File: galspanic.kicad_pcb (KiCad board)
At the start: 2 copper layers, 86.5 x 150 mm, 28 parts, among them J1 x68000_expansion, U1 CY62167E, U10 SN74AHCT245, U11 SN74AHCT245, U2 CY62167E, U3 CY62167E, U4 CY62167E, U5 ATF22V10C-10PU, U6 SN74AHCT245, U7 SN74AHCT245, U8 SN74AHCT245, U9 SN74AHCT245

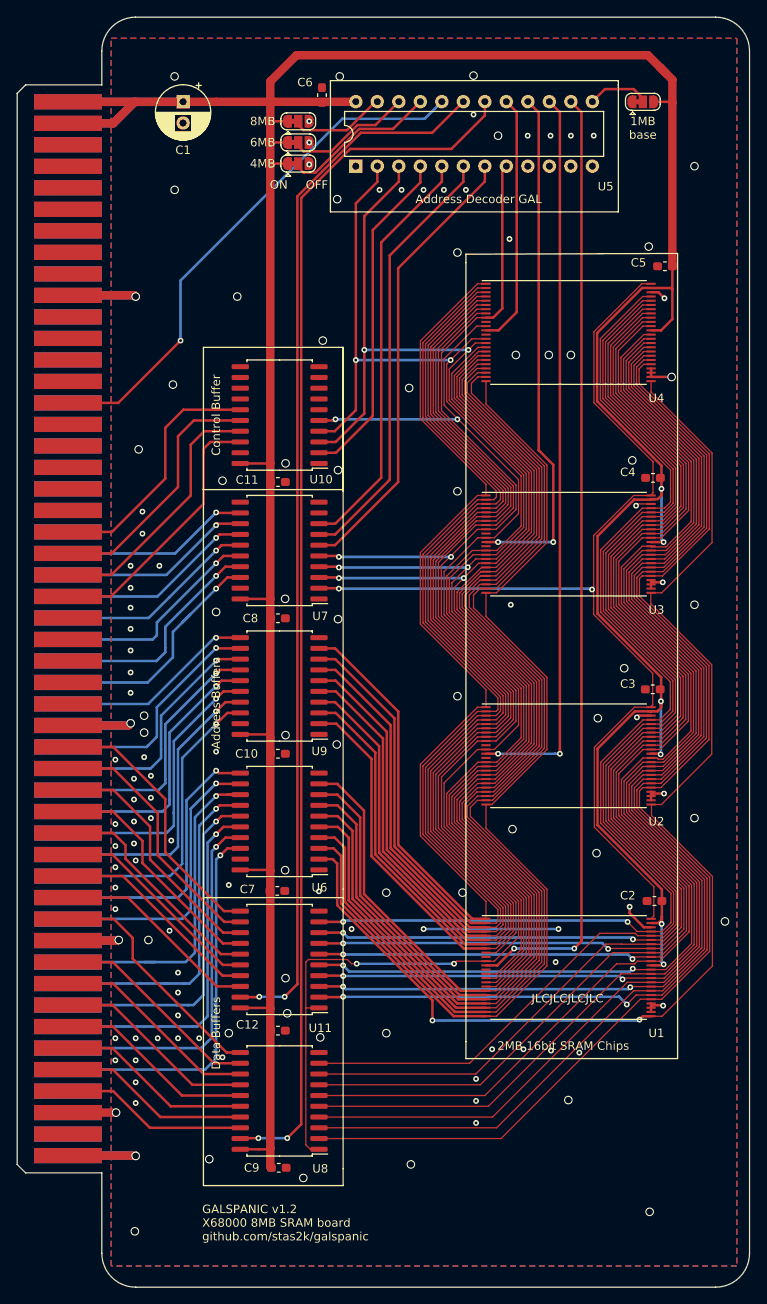
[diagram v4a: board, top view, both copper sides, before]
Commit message: release a smaller board with no buffers
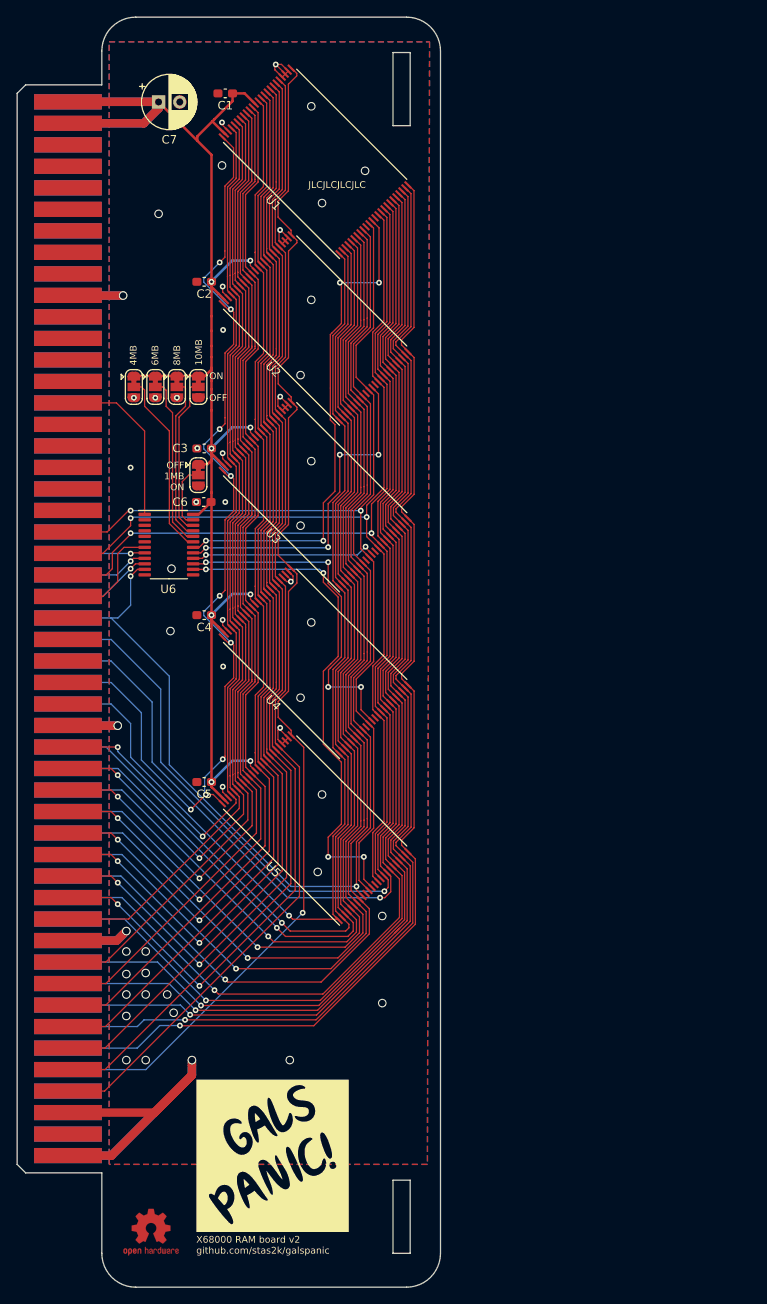
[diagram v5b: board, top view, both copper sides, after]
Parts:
- removed C10, C11, C12, C8, C9: 0.1uF, Capacitor_SMD:C_0603_1608Metric_Pad1.05x0.95mm_HandSolder
- removed U10, U11, U7, U8, U9: SN74AHCT245, Package_SO:SOIC-20W_7.5x12.8mm_P1.27mm
- added G***: LOGO, LOGO, F.Cu at (74.2, 173.5)
- added JP5: SolderJumper_3_Bridged12, Jumper:SolderJumper-3_P1.3mm_Bridged12_RoundedPad1.0x1.5mm, F.Cu at (65.4, 93.1)
- added REF**: OSHW-Logo2_7.3x6mm_Copper, Symbol:OSHW-Logo2_7.3x6mm_Copper, F.Cu at (59.8, 182.5)
- C1: value 220uF -> 0.1uF; footprint Capacitor_THT:CP_Radial_D6.3mm_P2.50mm -> Capacitor_SMD:C_0603_1608Metric_Pad1.08x0.95mm_HandSolder
- C2, C3, C4, C5, C6: footprint Capacitor_SMD:C_0603_1608Metric_Pad1.05x0.95mm_HandSolder -> Capacitor_SMD:C_0603_1608Metric_Pad1.08x0.95mm_HandSolder
- C7: value 0.1uF -> 220uF; footprint Capacitor_SMD:C_0603_1608Metric_Pad1.05x0.95mm_HandSolder -> Capacitor_THT:CP_Radial_D6.3mm_P2.50mm
- U5: value ATF22V10C-10PU -> CY62167E; footprint Package_DIP:DIP-24_W7.62mm -> Package_SO:TSOP-I-48_18.4x12mm_P0.5mm
- U6: value SN74AHCT245 -> ATF22V10C-10XU; footprint Package_SO:SOIC-20W_7.5x12.8mm_P1.27mm -> Package_SO:TSSOP-24_4.4x7.8mm_P0.65mm
- moved U1 99.8 mm to (79.2, 56.0), turned to 135 degrees
- moved C7 94.2 mm to (60.7, 49.0)
- moved C2 90.4 mm to (66.1, 70.3)
- moved C5 81.7 mm to (66.1, 129.3)
- moved U5 78.3 mm to (79.2, 134.7), turned to 135 degrees
- moved JP4 68.9 mm to (57.8, 82.7), turned to -90 degrees
- moved C3 60.1 mm to (66.1, 89.9)
- moved U2 58.8 mm to (79.2, 75.7), turned to 135 degrees
- moved C4 55.4 mm to (66.1, 109.6)
- moved C6 50.1 mm to (66.0, 96.3), turned to 180 degrees
- moved U4 49.0 mm to (79.2, 115.0), turned to 135 degrees
- moved U6 35.2 mm to (61.9, 101.3), turned to 0 degrees
- moved JP1 33.5 mm to (65.4, 82.7), turned to -90 degrees
- moved JP2 32.2 mm to (62.9, 82.7), turned to -90 degrees
- moved JP3 31.3 mm to (60.3, 82.7), turned to -90 degrees
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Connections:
- J1 pad A10: /DB6 -> /D6
- J1 pad A12: /DB7 -> /D7
- J1 pad A13: /DB8 -> /D8
- J1 pad A14: /DB9 -> /D9
- J1 pad A15: /DB10 -> /D10
- J1 pad A16: /DB11 -> /D11
- J1 pad A17: /DB12 -> /D12
- J1 pad A18: /DB13 -> /D13
- J1 pad A19: /DB14 -> /D14
- J1 pad A2: Net-(J1-PadA2) -> unconnected-(J1-PadA2)
- J1 pad A20: /DB15 -> /D15
- J1 pad A22: Net-(J1-PadA22) -> unconnected-(J1-PadA22)
- J1 pad A23: Net-(J1-PadA23) -> unconnected-(J1-PadA23)
- J1 pad A24: Net-(J1-PadA24) -> unconnected-(J1-PadA24)
- J1 pad A25: Net-(J1-PadA25) -> unconnected-(J1-PadA25)
- J1 pad A26: Net-(J1-PadA26) -> unconnected-(J1-PadA26)
- J1 pad A27: /B_#AS -> /~{AS}
- J1 pad A28: /B_#LDS -> /~{LDS}
- J1 pad A29: /B_#UDS -> /~{UDS}
- J1 pad A30: /B_R/W -> /~{R/}W
- J1 pad A31: no_connect_123 -> unconnected-(J1-PadA31)
- J1 pad A32: Net-(J1-PadA32) -> unconnected-(J1-PadA32)
- J1 pad A33: Net-(J1-PadA33) -> unconnected-(J1-PadA33)
- J1 pad A34: Net-(J1-PadA34) -> unconnected-(J1-PadA34)
- J1 pad A35: Net-(J1-PadA35) -> unconnected-(J1-PadA35)
- J1 pad A36: /B_#DTACK -> /~{DTACK}
- J1 pad A37: Net-(J1-PadA37) -> unconnected-(J1-PadA37)
- J1 pad A38: Net-(J1-PadA38) -> unconnected-(J1-PadA38)
- J1 pad A39: Net-(J1-PadA39) -> unconnected-(J1-PadA39)
- J1 pad A4: /DB0 -> /D0
- J1 pad A40: Net-(J1-PadA40) -> unconnected-(J1-PadA40)
- J1 pad A42: Net-(J1-PadA42) -> unconnected-(J1-PadA42)
- J1 pad A43: Net-(J1-PadA43) -> unconnected-(J1-PadA43)
- J1 pad A44: Net-(J1-PadA44) -> unconnected-(J1-PadA44)
- J1 pad A45: Net-(J1-PadA45) -> unconnected-(J1-PadA45)
- J1 pad A46: Net-(J1-PadA46) -> unconnected-(J1-PadA46)
- J1 pad A47: Net-(J1-PadA47) -> unconnected-(J1-PadA47)
- J1 pad A48: Net-(J1-PadA48) -> unconnected-(J1-PadA48)
- J1 pad A5: /DB1 -> /D1
- J1 pad A6: /DB2 -> /D2
- J1 pad A7: /DB3 -> /D3
- J1 pad A8: /DB4 -> /D4
- J1 pad A9: /DB5 -> /D5
- J1 pad B10: /AB6 -> /A6
- J1 pad B12: /AB7 -> /A7
- J1 pad B13: /AB8 -> /A8
- J1 pad B14: /AB9 -> /A9
- J1 pad B15: /AB10 -> /A10
- J1 pad B16: /AB11 -> /A11
- J1 pad B17: /AB12 -> /A12
- J1 pad B18: /AB13 -> /A13
- J1 pad B19: /AB14 -> /A14
- J1 pad B2: no_connect_124 -> unconnected-(J1-PadB2)
- J1 pad B20: /AB15 -> /A15
- J1 pad B22: /AB16 -> /A16
- J1 pad B23: /AB17 -> /A17
- J1 pad B24: /AB18 -> /A18
- J1 pad B25: /AB19 -> /A19
- J1 pad B26: /AB20 -> /A20
- J1 pad B27: /AB21 -> /A21
- J1 pad B28: /AB22 -> /A22
- J1 pad B29: /AB23 -> /A23
- J1 pad B3: no_connect_125 -> unconnected-(J1-PadB3)
- J1 pad B30: no_connect_126 -> unconnected-(J1-PadB30)
- J1 pad B31: no_connect_127 -> unconnected-(J1-PadB31)
- J1 pad B32: no_connect_128 -> unconnected-(J1-PadB32)
- J1 pad B33: no_connect_129 -> unconnected-(J1-PadB33)
- J1 pad B34: no_connect_130 -> unconnected-(J1-PadB34)
- J1 pad B35: no_connect_131 -> unconnected-(J1-PadB35)
- J1 pad B36: no_connect_132 -> unconnected-(J1-PadB36)
- J1 pad B37: no_connect_133 -> unconnected-(J1-PadB37)
- J1 pad B38: no_connect_134 -> unconnected-(J1-PadB38)
- J1 pad B39: no_connect_135 -> unconnected-(J1-PadB39)
- J1 pad B4: no_connect_136 -> unconnected-(J1-PadB4)
- J1 pad B40: no_connect_137 -> unconnected-(J1-PadB40)
- J1 pad B42: no_connect_138 -> unconnected-(J1-PadB42)
- J1 pad B43: no_connect_139 -> unconnected-(J1-PadB43)
- J1 pad B44: no_connect_140 -> unconnected-(J1-PadB44)
- J1 pad B45: no_connect_141 -> unconnected-(J1-PadB45)
- J1 pad B46: no_connect_142 -> unconnected-(J1-PadB46)
- J1 pad B47: no_connect_143 -> unconnected-(J1-PadB47)
- J1 pad B48: no_connect_144 -> unconnected-(J1-PadB48)
- J1 pad B5: /AB1 -> /A1
- J1 pad B6: /AB2 -> /A2
- J1 pad B7: /AB3 -> /A3
- J1 pad B8: /AB4 -> /A4
- J1 pad B9: /AB5 -> /A5
- JP1 pad 2: /MS8 -> /MS10
- JP2 pad 2: /MS6 -> /MS8
- JP3 pad 2: /MS4 -> /MS6
- JP4 pad 1: GND -> VCC
- JP4 pad 2: /MSK -> /MS4
- JP4 pad 3: VCC -> GND
- U1 pad 10: no_connect_145 -> unconnected-(U1-Pad10)
- U1 pad 11: /#R/W -> /~{R/}W
- U1 pad 13: no_connect_146 -> unconnected-(U1-Pad13)
- U1 pad 14: /#UDS -> /~{UDS}
- U1 pad 15: /#LDS -> /~{LDS}
- U2 pad 10: no_connect_150 -> unconnected-(U2-Pad10)
- U2 pad 11: /#R/W -> /~{R/}W
- U2 pad 13: no_connect_151 -> unconnected-(U2-Pad13)
- U2 pad 14: /#UDS -> /~{UDS}
- U2 pad 15: /#LDS -> /~{LDS}
- U3 pad 10: no_connect_152 -> unconnected-(U3-Pad10)
- U3 pad 11: /#R/W -> /~{R/}W
- U3 pad 13: no_connect_153 -> unconnected-(U3-Pad13)
- U3 pad 14: /#UDS -> /~{UDS}
- U3 pad 15: /#LDS -> /~{LDS}
- U4 pad 10: no_connect_154 -> unconnected-(U4-Pad10)
- U4 pad 11: /#R/W -> /~{R/}W
- U4 pad 13: no_connect_155 -> unconnected-(U4-Pad13)
- U4 pad 14: /#UDS -> /~{UDS}
- U4 pad 15: /#LDS -> /~{LDS}
- U5 pad 1: GND -> /A16
- U5 pad 10: GND -> unconnected-(U5-Pad10)
- U5 pad 11: GND -> /~{R/}W
- U5 pad 12: GND -> /CEM5
- U5 pad 13: /MSK -> unconnected-(U5-Pad13)
- U5 pad 14: /CEM1 -> /~{UDS}
- U5 pad 15: /CEM2 -> /~{LDS}
- U5 pad 16: /CEM3 -> /A19
- U5 pad 17: /CEM4 -> /A18
- U5 pad 18: /#CEL -> /A8
- U5 pad 19: /#CEH -> /A7
- U5 pad 2: /#UDS -> /A15
- U5 pad 20: /B_#DTACK -> /A6
- U5 pad 21: /MS4 -> /A5
- U5 pad 22: /MS6 -> /A4
- U5 pad 23: /MS8 -> /A3
- U5 pad 24: VCC -> /A2
- U5 pad 3: /#LDS -> /A14
- U5 pad 4: /#AS -> /A13
- U5 pad 5: /A23 -> /A12
- U5 pad 6: /A22 -> /A11
- U5 pad 7: /A21 -> /A10
- U5 pad 8: /A20 -> /A9
- U5 pad 9: GND -> /A20
- U6 pad 1: GND -> /~{DTACK}
- U6 pad 10: GND -> /A21
- U6 pad 11: /AB8 -> /A20
- U6 pad 12: /AB7 -> GND
- U6 pad 13: /AB6 -> GND
- U6 pad 14: /AB5 -> /CEM5
- U6 pad 15: /AB4 -> /CEM4
- U6 pad 16: /AB3 -> /CEM3
- U6 pad 17: /AB2 -> /CEM2
- U6 pad 18: /AB1 -> /CEM1
- U6 pad 19: GND -> /MS4
- U6 pad 2: /A1 -> GND
- U6 pad 20: VCC -> /MS6
- U6 pad 3: /A2 -> GND
- U6 pad 4: /A3 -> GND
- U6 pad 5: /A4 -> GND
- U6 pad 6: /A5 -> GND
- U6 pad 7: /A6 -> /~{AS}
- U6 pad 8: /A7 -> /A23
- U6 pad 9: /A8 -> /A22
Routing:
- net VCC: track 434.3 -> 194.3 mm, vias 6 -> 8
- net /#R/W: track 163.4 -> 0.00 mm, vias 4 -> 0
- net /#LDS: track 151.1 -> 0.00 mm, vias 2 -> 0
- net /#UDS: track 148.0 -> 0.00 mm, vias 2 -> 0
- net /#CEL: track 144.7 -> 0.00 mm, vias 2 -> 0
- net /#CEH: track 124.7 -> 0.00 mm, vias 2 -> 0
- net /~{LDS}: track 0.00 -> 122.7 mm, vias 0 -> 2
- net /~{UDS}: track 0.00 -> 121.4 mm, vias 0 -> 2
- net /~{R/}W: track 0.00 -> 120.5 mm, vias 0 -> 2
- net /B_#DTACK: track 63.1 -> 0.00 mm, vias 1 -> 0
- net /CEM5: track 0.00 -> 60.3 mm, vias 0 -> 4
- net /CEM1: track 112.2 -> 59.9 mm, vias 2 -> 4
- net /CEM2: track 87.0 -> 40.5 mm, vias 2 -> 4
- net /AB1: track 44.9 -> 0.00 mm, vias 1 -> 0
- net /AB2: track 43.5 -> 0.00 mm, vias 1 -> 0
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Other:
- board size 86.5 x 150 mm -> 50 x 150 mm
- board text added: "4MB 6MB 8MB 10MB"
- board text added: "OFF 1MB ON"
- board text added: "ON OFF"
- board text added: "X68000 RAM board v2 github.com/stas2k/galspanic"
- board text removed: "1MB base"
- board text removed: "2MB 16bit SRAM Chips"
- board text removed: "4MB"
- board text removed: "6MB"
- board text removed: "8MB"
- board text removed: "Address Buffers"
- board text removed: "Address Decoder GAL"
- board text removed: "Control Buffer"
- board text removed: "Data Buffers"
- board text removed: "GALSPANIC v1.2 X68000 8MB SRAM board github.com/stas2k/galspanic"
- board text removed: "OFF"
- board text removed: "ON"
